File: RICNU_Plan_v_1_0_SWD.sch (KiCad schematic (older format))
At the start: 8 parts, among them J7 FH19C-6S-0.5SH(05)

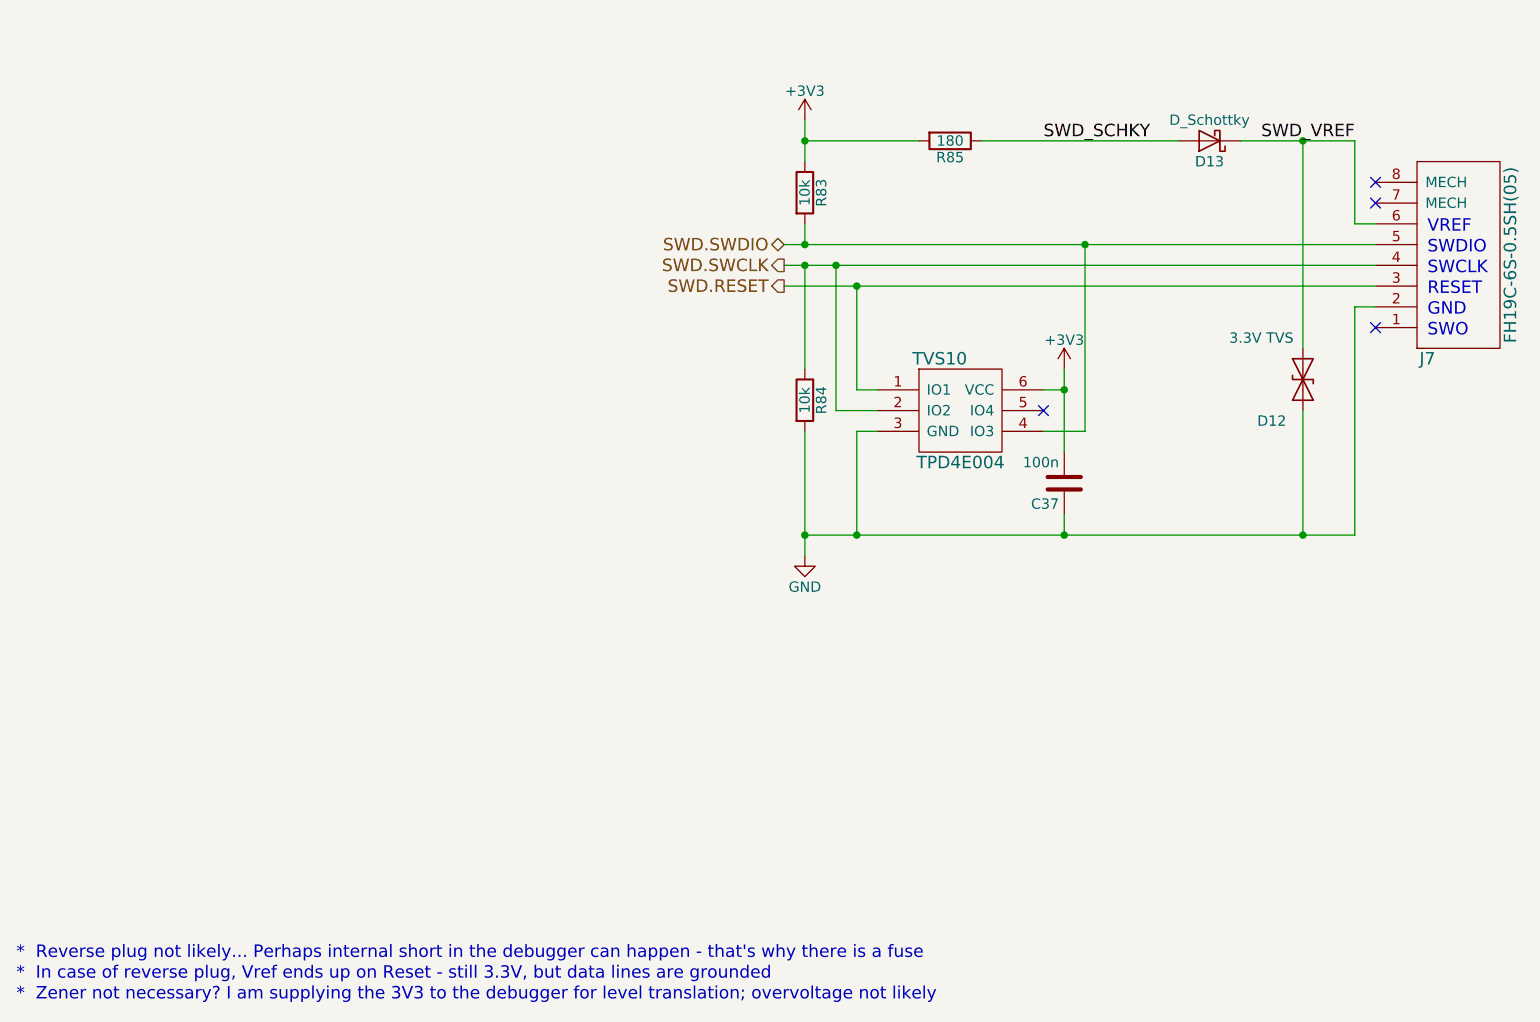
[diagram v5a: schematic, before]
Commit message: Deleting PDFs
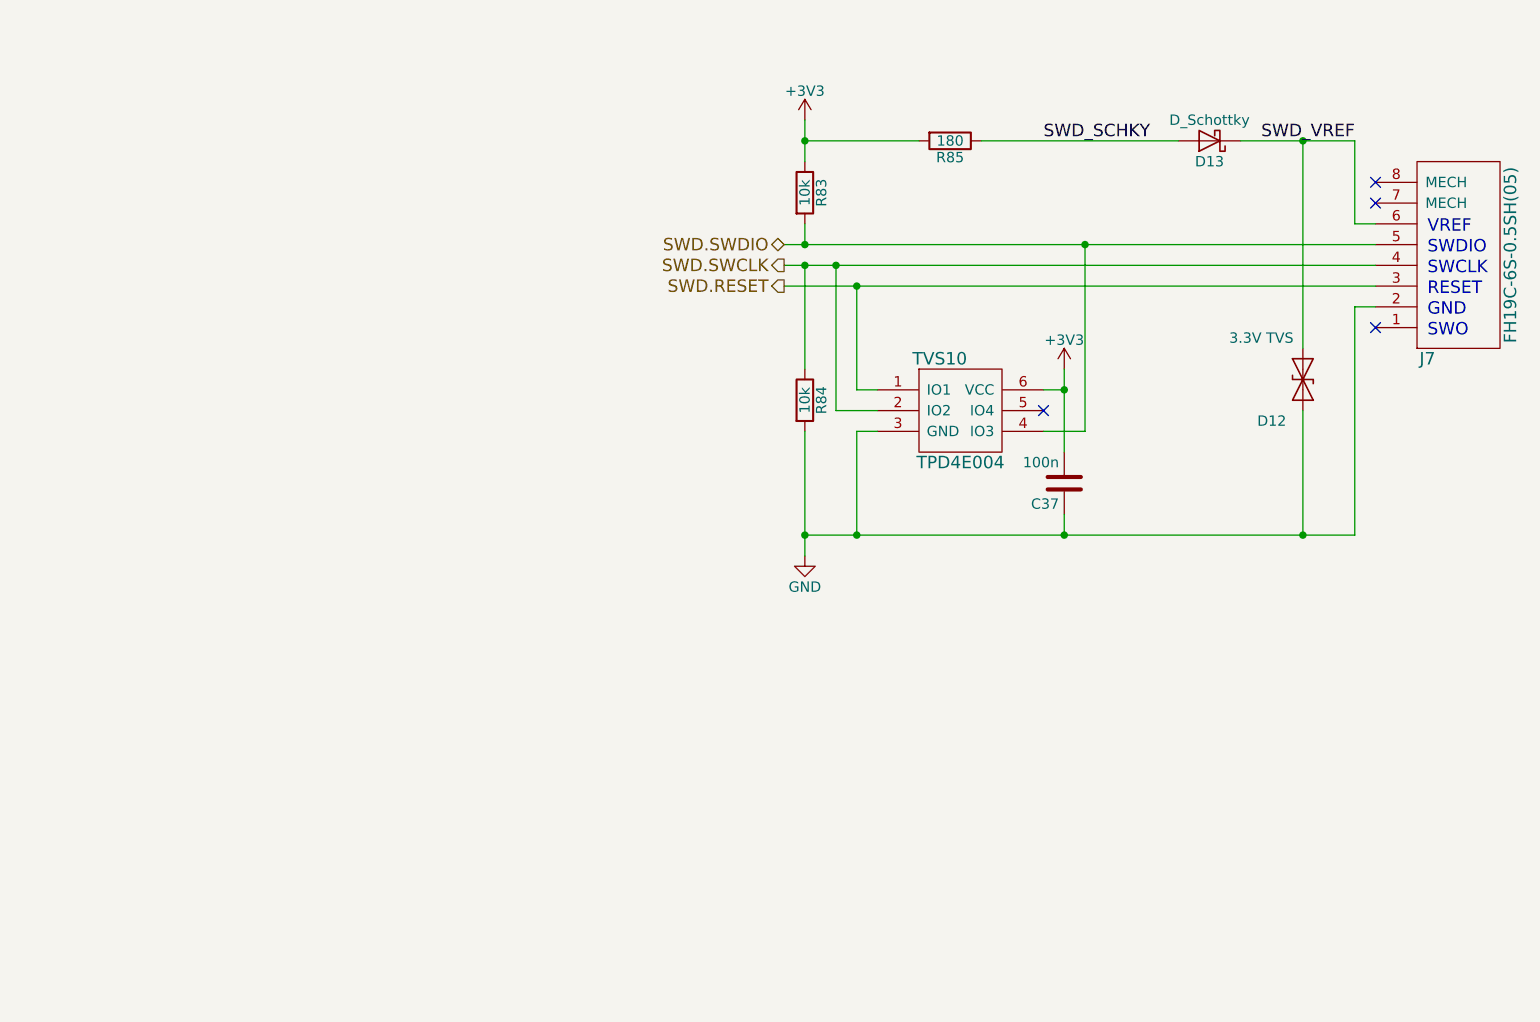
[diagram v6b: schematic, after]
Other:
- note removed: "* In case of reverse plug, Vref ends up on Reset - still 3.3V, but data lines are grounded"
- note removed: "* Reverse plug not likely... Perhaps internal short in the debugger can happen - that's why there is a fuse"
- note removed: "* Zener not necessary? I am supplying the 3V3 to the debugger for level translation; overvoltage not likely\n"
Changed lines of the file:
@@
 	1    0    0    -1
 $EndComp
-Text Notes 800  7050 0    60   ~ 0
-*  Reverse plug not likely... Perhaps internal short in the debugger can happen - that's why there is a fuse
-Text Notes 800  7150 0    60   ~ 0
-*  In case of reverse plug, Vref ends up on Reset - still 3.3V, but data lines are grounded
-Text Notes 800  7250 0    60   ~ 0
-*  Zener not necessary? I am supplying the 3V3 to the debugger for level translation; overvoltage not likely\n
 $Comp
 L D_Schottky D13
@@
 $EndComp
 Wire Wire Line
-	4500 3600 4600 3600
+	4500 3600 7350 3600
 Wire Wire Line
-	4600 3600 5950 3600
-Wire Wire Line
-	5950 3600 7350 3600
-Wire Wire Line
-	4500 3700 4600 3700
-Wire Wire Line
-	4600 3700 4750 3700
-Wire Wire Line
-	4750 3700 7350 3700
+	4500 3700 7350 3700
 Wire Wire Line
 	7250 3500 7350 3500
@@
 	6400 3100 5450 3100
 Wire Wire Line
-	4600 5000 4850 5000
-Wire Wire Line
-	4850 5000 5850 5000
-Wire Wire Line
-	5850 5000 7000 5000
-Wire Wire Line
-	7000 5000 7250 5000
+	4600 5000 7250 5000
 Wire Wire Line
 	7250 5000 7250 3900
@@
 	5750 4300 5850 4300
 Wire Wire Line
-	5850 4200 5850 4300
-Wire Wire Line
-	5850 4300 5850 4600
+	5850 4200 5850 4600
 Connection ~ 5850 4300
 Wire Wire Line
@@
 Connection ~ 5850 5000
 Wire Wire Line
-	4500 3800 4850 3800
-Wire Wire Line
-	4850 3800 7350 3800
+	4500 3800 7350 3800
 Connection ~ 4850 5000
 Wire Wire Line
@@
 Connection ~ 4600 3600
 Wire Wire Line
-	4600 3000 4600 3100
-Wire Wire Line
-	4600 3100 4600 3200
+	4600 3000 4600 3200
 Wire Wire Line
 	4600 3100 5150 3100
 Wire Wire Line
-	6700 3100 7000 3100
-Wire Wire Line
-	7000 3100 7250 3100
+	6700 3100 7250 3100
 Connection ~ 4600 3100
 Wire Wire Line
 	4850 4500 4850 5000
 Wire Wire Line
-	4600 4500 4600 5000
-Wire Wire Line
-	4600 5000 4600 5100
+	4600 4500 4600 5100
 Connection ~ 4600 5000
 Text Notes 7600 3550 0    60   ~ 0
